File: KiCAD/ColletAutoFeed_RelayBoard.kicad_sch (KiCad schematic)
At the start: 3 parts, among them J1 1761685-6, J2 2068320202, U1 ProS3

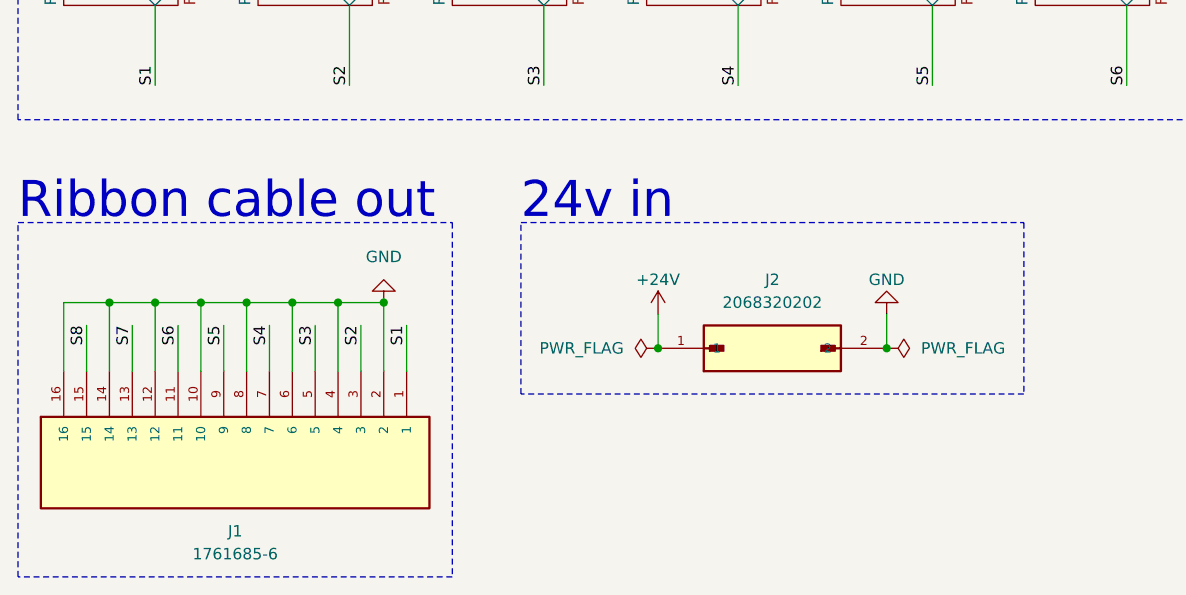
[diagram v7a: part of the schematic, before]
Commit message: Combined 2 pin power input into ribbon cable
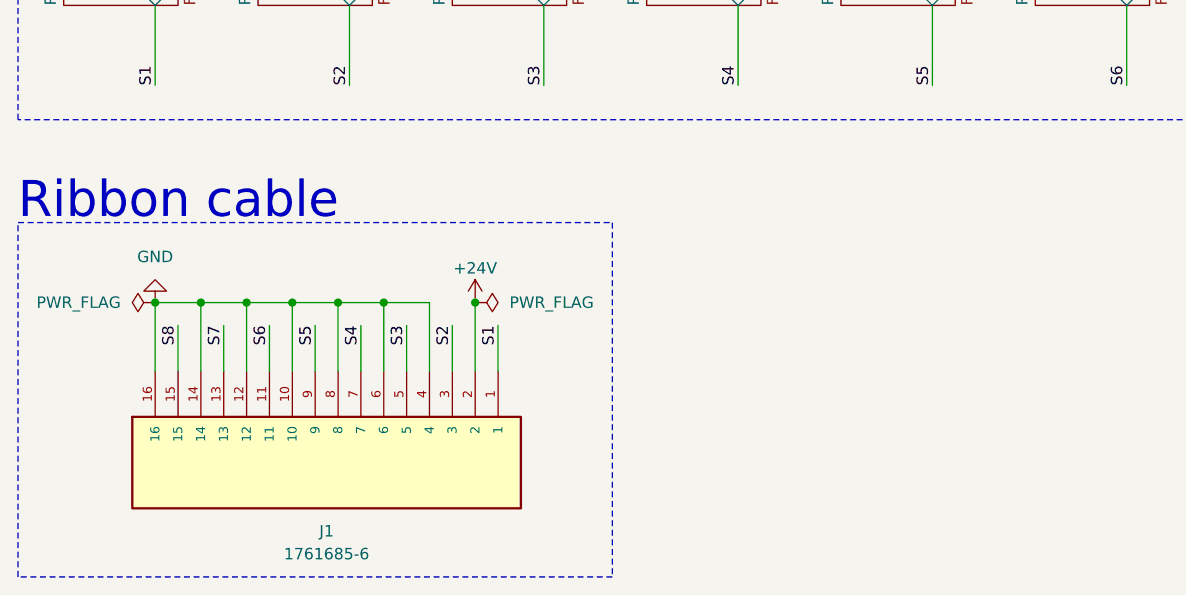
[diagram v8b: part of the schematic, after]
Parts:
- removed J2: 2068320202, Molex 206832-0202:MOLEX_2068320202, symbol Molex 206832-0202:2068320202
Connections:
- net +24V: now also J1.2
- net GND: no longer J1.2
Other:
- note added: "Ribbon cable"
- note removed: "24v in"
- note removed: "Ribbon cable out"
- moved on the sheet: J1
